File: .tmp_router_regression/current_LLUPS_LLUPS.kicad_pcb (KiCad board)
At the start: 2 copper layers, 140 x 90 mm, 39 parts, among them J1 USB_C, J2 Output, J3 Debug, Q1 FS8205A, U1 USBLC6-2SC6, U2 BQ24072, U3 HY2113-KB5B, U4 MT3608, U5 AP2112K-3.3, U6 LN61CN3302MR-G

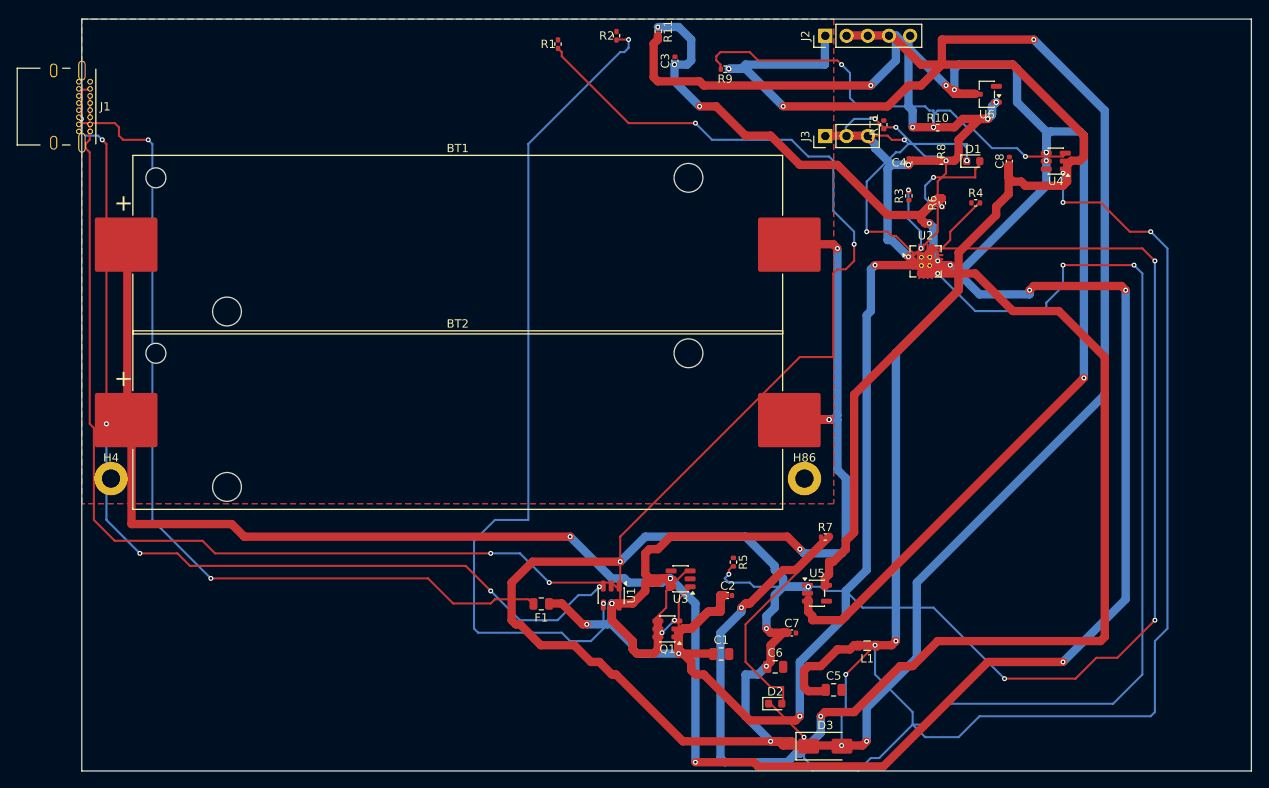
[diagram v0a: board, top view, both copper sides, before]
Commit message: 45-round experiment: best score 25.66, all nets routed (26/26)
Fixed A* performance by increasing max_search from 100k->500k to handle
high trace costs (100.0) without timing out. Kept high cost + coarse grid
(0.5mm) to prevent shorts while still routing efficiently.

Best config: edge_margin=5.7493mm, cooling_factor=0.9764, existing_trace_cost=200, max_rips=8

Co-Authored-By: Claude Opus 4.6 <noreply@anthropic.com>
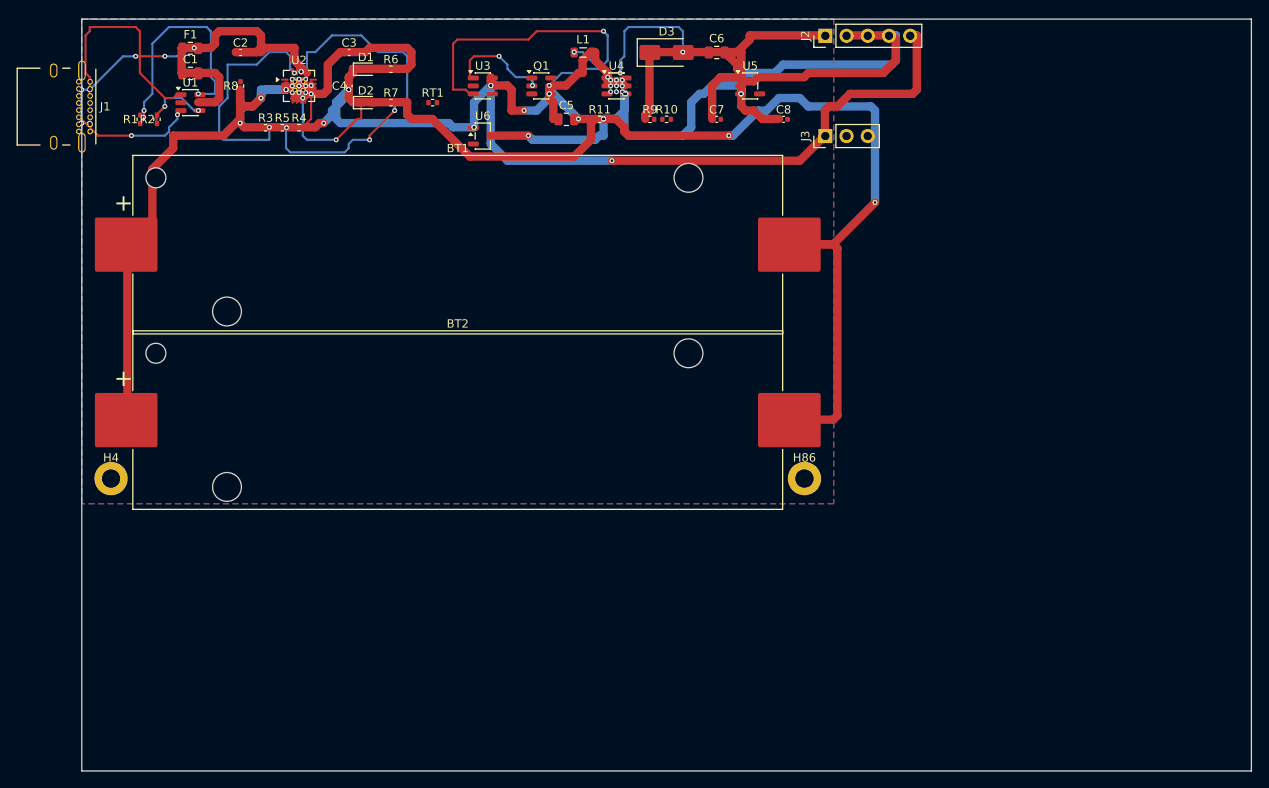
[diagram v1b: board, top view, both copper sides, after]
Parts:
- moved C1 94.2 mm to (13.0, 6.50)
- moved C2 87.3 mm to (19.0, 4.00)
- moved D2 87.0 mm to (34.0, 10.0)
- moved D3 85.2 mm to (70.0, 4.00)
- moved R8 84.4 mm to (19.0, 8.00), turned to 90 degrees
- moved R4 81.5 mm to (26.0, 13.0)
- moved L1 78.7 mm to (60.0, 4.00), turned to 0 degrees
- moved F1 78.7 mm to (13.0, 3.50), turned to 0 degrees
- moved U2 77.9 mm to (26.0, 8.00)
- moved U1 77.6 mm to (13.0, 10.0), turned to 0 degrees
- moved R3 77.4 mm to (22.0, 13.0), turned to 0 degrees
- moved C5 75.4 mm to (58.0, 12.0)
- moved R5 75.0 mm to (24.0, 13.0), turned to 0 degrees
- moved C6 73.9 mm to (76.0, 4.00)
- moved R7 73.5 mm to (37.0, 10.0)
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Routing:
- net /5V: track 286.0 -> 46.1 mm, vias 12 -> 0
- net /VSYS: track 209.9 -> 69.2 mm, vias 8 -> 2
- net /VBAT: track 315.3 -> 180.2 mm, vias 18 -> 12
- net Net-(D2-K): track 134.1 -> 14.7 mm, vias 4 -> 2
- net Net-(D3-A): track 131.0 -> 22.1 mm, vias 6 -> 4
- net /VBUS: track 142.8 -> 39.6 mm, vias 6 -> 0
- net Net-(J1-CC2): track 116.8 -> 14.7 mm, vias 6 -> 2
- net Net-(R2-Pad1): track 102.0 -> 8.04 mm
- net Net-(J1-CC1): track 117.9 -> 26.1 mm, vias 2 -> 0
- net /EN: track 160.7 -> 70.1 mm
- net Net-(U2-TMR): track 131.9 -> 42.3 mm, vias 4 -> 5
- net Net-(F1-Pad2): track 110.2 -> 21.1 mm, vias 2 -> 10
- net Net-(R1-Pad1): track 107.4 -> 27.9 mm
- net /3V3: track 109.4 -> 36.4 mm
- net /VSYS_BOOST: track 82.1 -> 18.8 mm, vias 2 -> 0
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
